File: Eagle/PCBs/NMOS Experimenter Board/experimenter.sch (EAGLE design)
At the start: 1182 parts, among them Q10 2N7002, Q11 2N7002, Q12 2N7002, Q13 2N7002, Q14 2N7002, Q15 2N7002, Q16 2N7002, Q17 2N7002, Q18 2N7002, Q19 2N7002, Q2 2N7002, Q20 2N7002, Q21 2N7002, Q22 2N7002, Q23 2N7002, Q24 2N7002, Q25 2N7002, Q26 2N7002, Q27 2N7002, Q28 2N7002, Q29 2N7002, Q3 2N7002, Q30 2N7002, Q31 2N7002, Q32 2N7002, Q33 2N7002, Q34 2N7002, Q35 2N7002, Q36 2N7002, Q37 2N7002, Q38 2N7002, Q39 2N7002, Q4 2N7002, Q40 2N7002, Q41 2N7002, Q42 2N7002, Q43 2N7002, Q44 2N7002, Q45 2N7002, Q46 2N7002, Q47 2N7002, Q48 2N7002, Q49 2N7002, Q5 2N7002, Q50 2N7002, Q51 2N7002, Q52 2N7002, Q53 2N7002, Q54 2N7002, Q55 2N7002, Q56 2N7002, Q57 2N7002, Q58 2N7002, Q59 2N7002, Q6 2N7002, Q60 2N7002, Q61 2N7002, Q62 2N7002, Q63 2N7002, Q64 2N7002, Q65 2N7002, Q66 2N7002, Q67 2N7002, Q68 2N7002, Q69 2N7002, Q7 2N7002, Q70 2N7002, Q71 2N7002, Q72 2N7002, Q73 2N7002, Q8 2N7002, Q9 2N7002, U1 74HC14PW

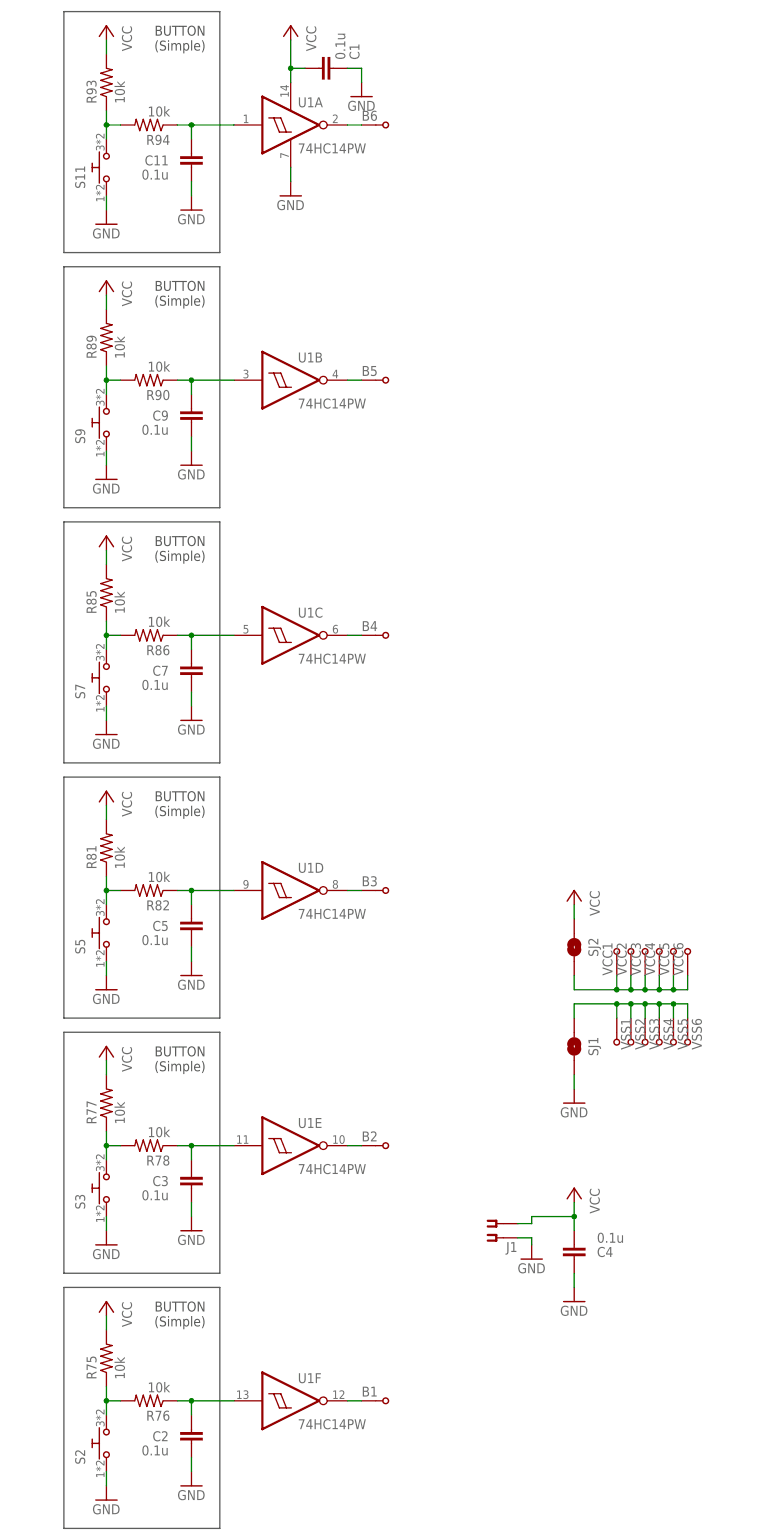
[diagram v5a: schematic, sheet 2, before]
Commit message: Added switches, preemptive first version
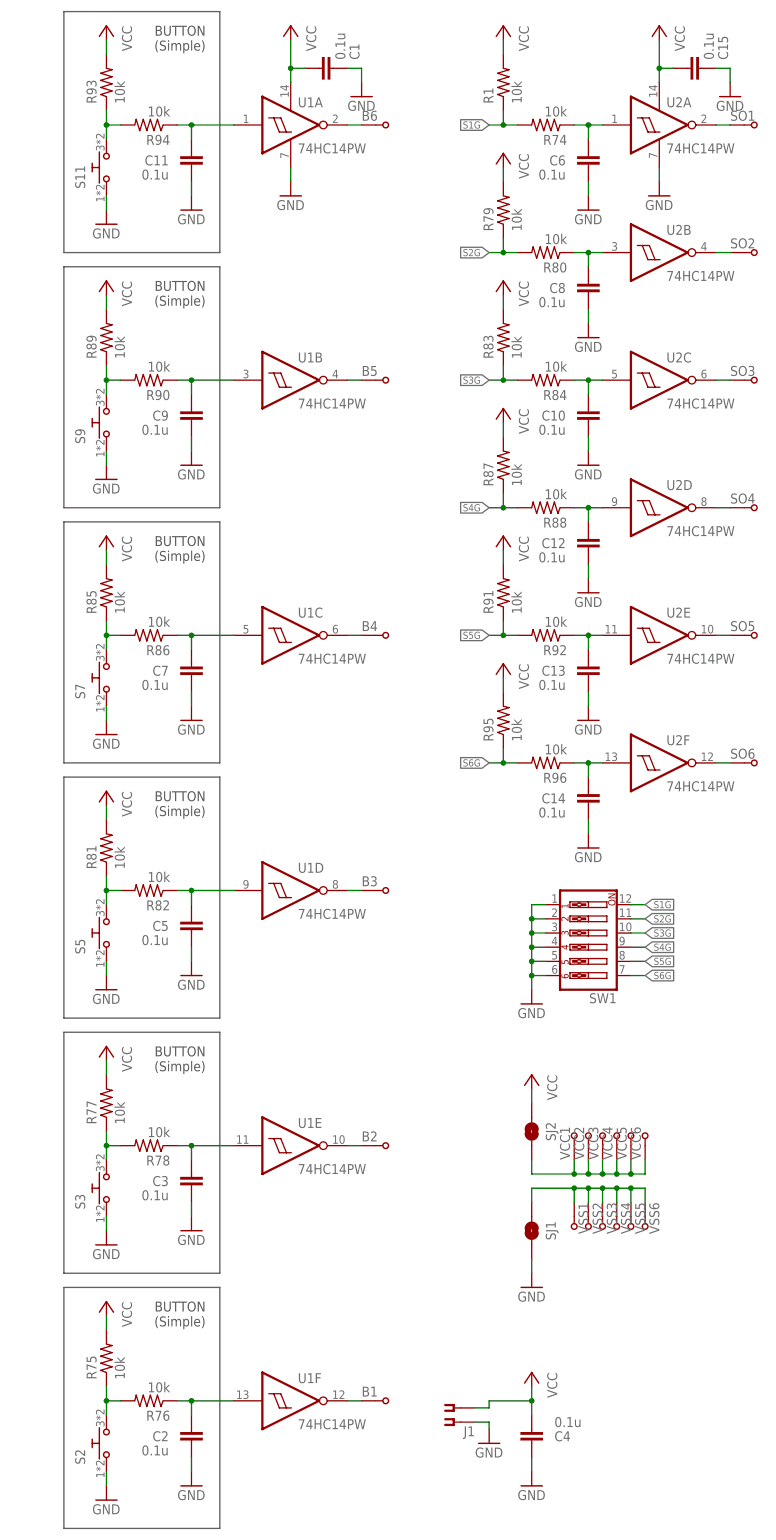
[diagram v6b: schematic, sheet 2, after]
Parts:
- added C10, C12, C13, C14, C15, C6, C8: 0.1u, ellajameson-core:CAP0603
- added R1, R74, R79, R80, R83, R84, R87, R88, R91, R92, R95, R96: 10k, ellajameson-core:RES0603
- added SO1, SO2, SO3, SO4, SO5, SO6: TPWIRE, ellajameson-core:TPWIRE
- added SW1: (no value), ellajameson-core:SW_DIP-6
- added U2: 74HC14PW, ellajameson-core:74HC14PW
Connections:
- new net N$307: SO6.S, U2F.O
- new net N$308: SO5.S, U2E.O
- new net N$311: SO4.S, U2D.O
- new net N$312: C8.1, R80.1, U2B.I
- new net N$313: SO3.S, U2C.O
- new net N$314: C10.1, R84.1, U2C.I
- new net N$315: SO2.S, U2B.O
- new net N$316: C12.1, R88.1, U2D.I
- new net N$317: SO1.S, U2A.O
- new net N$318: C13.1, R92.1, U2E.I
- new net N$320: C14.1, R96.1, U2F.I
- new net S1F: C6.1, R74.1, U2A.I
- new net S1G: R1.1, R74.2, SW1.12
- new net S2G: R79.1, R80.2, SW1.11
- new net S3G: R83.1, R84.2, SW1.10
- new net S4G: R87.1, R88.2, SW1.9
- new net S5G: R91.1, R92.2, SW1.8
- new net S6G: R95.1, R96.2, SW1.7
- net GND: now also C10.2, C12.2, C13.2, C14.2, C15.2, C6.2, C8.2, SW1.1, SW1.2, SW1.3, SW1.4, SW1.5, SW1.6, U2G$1.V-
- net VCC: now also C15.1, R1.2, R79.2, R83.2, R87.2, R91.2, R95.2, U2G$1.V+
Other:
- moved on the sheet: C4, J1, SJ1, SJ2, VCC1, VCC2, VCC3, VCC4, VCC5, VCC6, VSS1, VSS2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

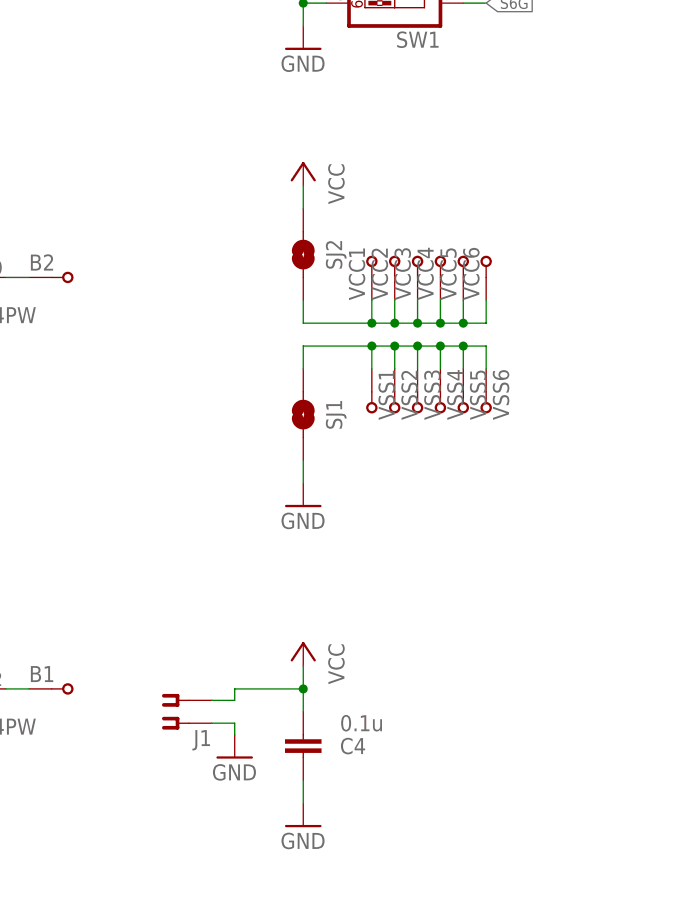
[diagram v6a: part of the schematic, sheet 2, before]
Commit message: Added amazing protoboard area.
https://www.eevblog.com/forum/manufacture/improved-protoboardperfboard-for-direct-soic-mounting/
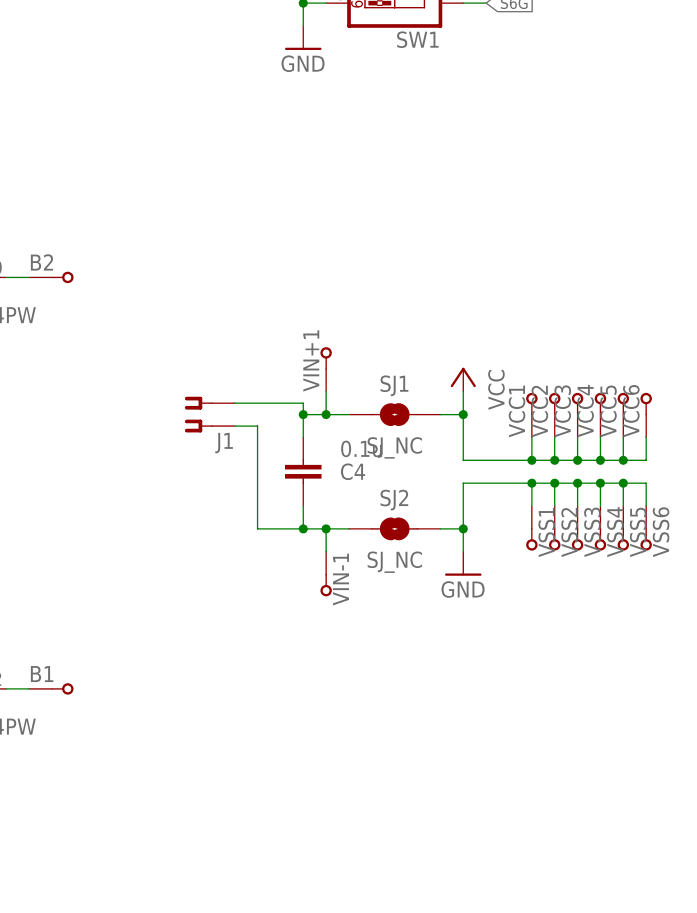
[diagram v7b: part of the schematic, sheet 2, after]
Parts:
- added VIN+1, VIN-1: TPWIRE, ellajameson-core:TPWIRE
- SJ1, SJ2: value SJ_NO -> SJ_NC; device ellajameson-core:SJ_NO -> ellajameson-core:SJ_NC
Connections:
- removed net N$303: SJ2.2, VCC1.S, VCC2.S, VCC3.S, VCC4.S, VCC5.S, VCC6.S
- removed net N$304: SJ1.1, VSS1.S, VSS2.S, VSS3.S, VSS4.S, VSS5.S, VSS6.S
- new net N$321: C4.1, J1.S, SJ2.1, VIN-1.S
- new net N$322: C4.2, J1.S1, SJ1.1, VIN+1.S
- net GND: now also SJ2.2, VSS1.S, VSS2.S, VSS3.S, VSS4.S, VSS5.S, VSS6.S; no longer C4.1, J1.S, SJ1.2
- net VCC: now also SJ1.2, VCC1.S, VCC2.S, VCC3.S, VCC4.S, VCC5.S, VCC6.S; no longer C4.2, J1.S1, SJ2.1
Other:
- moved on the sheet: C4, J1, SJ1, SJ2, VCC1, VCC2, VCC3, VCC4, VCC5, VCC6, VSS1, VSS2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

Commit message: Start rework on experimenter
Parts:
- removed C10, C12, C13, C14, C15, C6, C8: 0.1u, ellajameson-core:CAP0603
- removed D10, D11, D12, D13, D14, D15, D16, D17, D18, D19, D2, D20, D21, D22, D23, D24, D25, D26, D27, D28, D29, D3, D30, D31, D32, D33, D34, D35, D36, D37, D38, D39, D4, D40, D41, D42, D43, D44, D45, D46, D47, D48, D49, D5, D50, D51, D52, D53, D54, D55, D56, D57, D58, D59, D6, D60, D61, D62, D63, D64, D65, D66, D67, D68, D69, D7, D70, D71, D72, D73, D8, D9: (no value), ellajameson-core:LED0603
- removed DRAINA10, DRAINA11, DRAINA12, DRAINA13, DRAINA14, DRAINA15, DRAINA16, DRAINA17, DRAINA18, DRAINA19, DRAINA2, DRAINA20, DRAINA21, DRAINA22, DRAINA23, DRAINA24, DRAINA25, DRAINA26, DRAINA27, DRAINA28, DRAINA29, DRAINA3, DRAINA30, DRAINA31, DRAINA32, DRAINA33, DRAINA34, DRAINA35, DRAINA36, DRAINA37, DRAINA38, DRAINA39, DRAINA4, DRAINA40, DRAINA41, DRAINA42, DRAINA43, DRAINA44, DRAINA45, DRAINA46, DRAINA47, DRAINA48, DRAINA49, DRAINA5, DRAINA50, DRAINA51, DRAINA52, DRAINA53, DRAINA54, DRAINA55, DRAINA56, DRAINA57, DRAINA58, DRAINA59, DRAINA6, DRAINA60, DRAINA61, DRAINA62, DRAINA63, DRAINA64, DRAINA65, DRAINA66, DRAINA67, DRAINA68, DRAINA69, DRAINA7, DRAINA70, DRAINA71, DRAINA72, DRAINA73, DRAINA8, DRAINA9, DRAINB10, DRAINB11, DRAINB12, DRAINB13, DRAINB14, DRAINB15, DRAINB16, DRAINB17, DRAINB18, DRAINB19, DRAINB2, DRAINB20, DRAINB21, DRAINB22, DRAINB23, DRAINB24, DRAINB25, DRAINB26, DRAINB27, DRAINB28, DRAINB29, DRAINB3, DRAINB30, DRAINB31, DRAINB32, DRAINB33, DRAINB34, DRAINB35, DRAINB36, DRAINB37, DRAINB38, DRAINB39, DRAINB4, DRAINB40, DRAINB41, DRAINB42, DRAINB43, DRAINB44, DRAINB45, DRAINB46, DRAINB47, DRAINB48, DRAINB49, DRAINB5, DRAINB50, DRAINB51, DRAINB52, DRAINB53, DRAINB54, DRAINB55, DRAINB56, DRAINB57, DRAINB58, DRAINB59, DRAINB6, DRAINB60, DRAINB61, DRAINB62, DRAINB63, DRAINB64, DRAINB65, DRAINB66, DRAINB67, DRAINB68, DRAINB69, DRAINB7, DRAINB70, DRAINB71, DRAINB72, DRAINB73, DRAINB8, DRAINB9, DRAINC10, DRAINC11, DRAINC12, DRAINC13, DRAINC14, DRAINC15, DRAINC16, DRAINC17, DRAINC18, DRAINC19, DRAINC2, DRAINC20, DRAINC21, DRAINC22, DRAINC23, DRAINC24, DRAINC25, DRAINC26, DRAINC27, DRAINC28, DRAINC29, DRAINC3, DRAINC30, DRAINC31, DRAINC32, DRAINC33, DRAINC34, DRAINC35, DRAINC36, DRAINC37, DRAINC38, DRAINC39, DRAINC4, DRAINC40, DRAINC41, DRAINC42, DRAINC43, DRAINC44, DRAINC45, DRAINC46, DRAINC47, DRAINC48, DRAINC49, DRAINC5, DRAINC50, DRAINC51, DRAINC52, DRAINC53, DRAINC54, DRAINC55, DRAINC56, DRAINC57, DRAINC58, DRAINC59, DRAINC6, DRAINC60, DRAINC61, DRAINC62, DRAINC63, DRAINC64, DRAINC65, DRAINC66, DRAINC67, DRAINC68, DRAINC69, DRAINC7, DRAINC70, DRAINC71, DRAINC72, DRAINC73, DRAINC8, DRAINC9, DRAIND10, DRAIND11, DRAIND12, DRAIND13, DRAIND14, DRAIND15, DRAIND16, DRAIND17, DRAIND18, DRAIND19, DRAIND2, DRAIND20, DRAIND21, DRAIND22, DRAIND23, DRAIND24, DRAIND25, DRAIND26, DRAIND27, DRAIND28, DRAIND29, DRAIND3, DRAIND30, DRAIND31, DRAIND32, DRAIND33, DRAIND34, DRAIND35, DRAIND36, DRAIND37, DRAIND38, DRAIND39, DRAIND4, DRAIND40, DRAIND41, DRAIND42, DRAIND43, DRAIND44, DRAIND45, DRAIND46, DRAIND47, DRAIND48, DRAIND49, DRAIND5, DRAIND50, DRAIND51, DRAIND52, DRAIND53, DRAIND54, DRAIND55, DRAIND56, DRAIND57, DRAIND58, DRAIND59, DRAIND6, DRAIND60, DRAIND61, DRAIND62, DRAIND63, DRAIND64, DRAIND65, DRAIND66, DRAIND67, DRAIND68, DRAIND69, DRAIND7, DRAIND70, DRAIND71, DRAIND72, DRAIND73, DRAIND8, DRAIND9, GATE10, GATE11, GATE12, GATE13, GATE14, GATE15, GATE16, GATE17, GATE18, GATE19, GATE2, GATE20, GATE21, GATE22, GATE23, GATE24, GATE25, GATE26, GATE27, GATE28, GATE29, GATE3, GATE30, GATE31, GATE32, GATE33, GATE34, GATE35, GATE36, GATE37, GATE38, GATE39, GATE4, GATE40, GATE41, GATE42, GATE43, GATE44, GATE45, GATE46, GATE47, GATE48, GATE49, GATE5, GATE50, GATE51, GATE52, GATE53, GATE54, GATE55, GATE56, GATE57, GATE58, GATE59, GATE6, GATE60, GATE61, GATE62, GATE63, GATE64, GATE65, GATE66, GATE67, GATE68, GATE69, GATE7, GATE70, GATE71, GATE72, GATE73, GATE8, GATE9, SO1, SO2, SO3, SO4, SO5, SO6, SOURCEA10, SOURCEA11, SOURCEA12, SOURCEA13, SOURCEA14, SOURCEA15, SOURCEA16, SOURCEA17, SOURCEA18, SOURCEA19, SOURCEA2, SOURCEA20, SOURCEA21, SOURCEA22, SOURCEA23, SOURCEA24, SOURCEA25, SOURCEA26, SOURCEA27, SOURCEA28, SOURCEA29, SOURCEA3, SOURCEA30, SOURCEA31, SOURCEA32, SOURCEA33, SOURCEA34, SOURCEA35, SOURCEA36, SOURCEA37, SOURCEA38, SOURCEA39, SOURCEA4, SOURCEA40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: TPWIRE, ellajameson-core:TPWIRE
- removed JD10, JD11, JD12, JD13, JD14, JD17, JD18, JD19, JD2, JD20, JD21, JD22, JD23, JD24, JD25, JD26, JD27, JD28, JD29, JD3, JD30, JD31, JD32, JD33, JD34, JD35, JD36, JD37, JD38, JD39, JD4, JD40, JD41, JD42, JD43, JD44, JD45, JD46, JD47, JD48, JD49, JD5, JD50, JD51, JD52, JD53, JD54, JD55, JD56, JD57, JD58, JD59, JD6, JD60, JD61, JD62, JD63, JD64, JD65, JD66, JD68, JD7, JD70, JD72, JD8, JD9, JN10, JN11, JN12, JN13, JN14, JN15, JN16, JN17, JN18, JN19, JN2, JN20, JN21, JN22, JN23, JN24, JN25, JN26, JN27, JN28, JN29, JN3, JN30, JN31, JN32, JN33, JN34, JN35, JN36, JN37, JN38, JN39, JN4, JN40, JN41, JN42, JN43, JN44, JN45, JN46, JN47, JN48, JN49, JN5, JN50, JN51, JN52, JN53, JN54, JN55, JN56, JN57, JN58, JN59, JN6, JN60, JN61, JN62, JN63, JN64, JN65, JN66, JN67, JN68, JN69, JN7, JN70, JN71, JN72, JN73, JN8, JN9, JP10, JP11, JP12, JP13, JP14, JP15, JP16, JP17, JP18, JP19, JP2, JP20, JP21, JP22, JP23, JP24, JP25, JP26, JP27, JP28, JP29, JP3, JP30, JP31, JP32, JP33, JP34, JP35, JP36, JP37, JP38, JP39, JP4, JP40, JP41, JP42, JP43, JP44, JP45, JP46, JP47, JP48, JP49, JP5, JP50, JP51, JP52, JP53, JP54, JP55, JP56, JP57, JP58, JP59, JP6, JP60, JP61, JP62, JP63, JP64, JP65, JP66, JP67, JP68, JP69, JP7, JP70, JP71, JP72, JP73, JP8, JP9, JS10, JS11, JS12, JS13, JS16, JS17, JS26, JS27, JS28, JS29, JS30, JS31, JS32, JS33, JS34, JS35, JS36, JS37, JS38, JS39, JS4, JS40, JS41, JS42, JS43, JS44, JS45, JS46, JS47, JS48, JS49, JS5, JS50, JS51, JS52, JS53, JS54, JS55, JS56, JS57, JS58, JS59, JS6, JS60, JS61, JS62, JS63, JS64, JS65, JS66, JS67, JS68, JS69, JS7, JS70, JS71, JS72, JS73, JS8, JS9: SJ_NO, ellajameson-core:SJ_NO
- removed Q10, Q11, Q12, Q13, Q14, Q15, Q16, Q17, Q18, Q19, Q2, Q20, Q21, Q22, Q23, Q24, Q25, Q26, Q27, Q28, Q29, Q3, Q30, Q31, Q32, Q33, Q34, Q35, Q36, Q37, Q38, Q39, Q4, Q40, Q41, Q42, Q43, Q44, Q45, Q46, Q47, Q48, Q49, Q5, Q50, Q51, Q52, Q53, Q54, Q55, Q56, Q57, Q58, Q59, Q6, Q60, Q61, Q62, Q63, Q64, Q65, Q66, Q67, Q68, Q69, Q7, Q70, Q71, Q72, Q73, Q8, Q9: 2N7002, ellajameson-core:2N7002
- removed R1, R74, R79, R80, R83, R84, R87, R88, R91, R92, R95, R96: 10k, ellajameson-core:RES0603
- removed R10, R11, R12, R13, R14, R15, R16, R17, R18, R19, R2, R20, R21, R22, R23, R24, R25, R26, R27, R28, R29, R3, R30, R31, R32, R33, R34, R35, R36, R37, R38, R39, R4, R40, R41, R42, R43, R44, R45, R46, R47, R48, R49, R5, R50, R51, R52, R53, R54, R55, R56, R57, R58, R59, R6, R60, R61, R62, R63, R64, R65, R66, R67, R68, R69, R7, R70, R71, R72, R73, R8, R9: (no value), ellajameson-core:RES0603
- removed U2: 74HC14PW, ellajameson-core:74HC14PW
- B1, B2, B3, B4, B5, B6, VCC1, VCC2, VCC3, VIN+1, VIN-1, VSS1, VSS2, VSS3: value TPWIRE -> TPTHT; device ellajameson-core:TPWIRE -> ellajameson-core:TPTHT
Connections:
- removed net N$1: D2.A, JP2.2, R2.1
- removed net N$10: D3.K, DRAINA3.S, DRAINB3.S, DRAINC3.S, DRAIND3.S, JD2.1, JD3.2, JP3.1, JS5.1, Q3.D
- removed net N$100: GATE25.S, Q25.G
- removed net N$101: D26.A, JP26.2, R26.1
- removed net N$102: D26.K, DRAINA26.S, DRAINB26.S, DRAINC26.S, DRAIND26.S, JD26.2, JP26.1, JS34.1, Q26.D
- removed net N$103: JN26.2, JS26.2, Q26.S, SOURCEA26.S, SOURCEB26.S, SOURCEC26.S, SOURCED26.S
- removed net N$104: GATE26.S, Q26.G
- removed net N$105: D27.A, JP27.2, R27.1
- removed net N$106: D27.K, DRAINA27.S, DRAINB27.S, DRAINC27.S, DRAIND27.S, JD26.1, JD27.2, JP27.1, JS35.1, Q27.D
- removed net N$107: JN27.2, JS27.2, Q27.S, SOURCEA27.S, SOURCEB27.S, SOURCEC27.S, SOURCED27.S
- removed net N$108: GATE27.S, Q27.G
- removed net N$109: D28.A, JP28.2, R28.1
- removed net N$11: JN3.2, Q3.S, SOURCEA3.S, SOURCEB3.S, SOURCEC3.S, SOURCED3.S
- removed net N$110: D28.K, DRAINA28.S, DRAINB28.S, DRAINC28.S, DRAIND28.S, JD27.1, JD28.2, JP28.1, JS36.1, Q28.D
- removed net N$111: JN28.2, JS28.2, Q28.S, SOURCEA28.S, SOURCEB28.S, SOURCEC28.S, SOURCED28.S
- removed net N$112: GATE28.S, Q28.G
- removed net N$113: D29.A, JP29.2, R29.1
- removed net N$114: D29.K, DRAINA29.S, DRAINB29.S, DRAINC29.S, DRAIND29.S, JD28.1, JD29.2, JP29.1, JS37.1, Q29.D
- removed net N$115: JN29.2, JS29.2, Q29.S, SOURCEA29.S, SOURCEB29.S, SOURCEC29.S, SOURCED29.S
- removed net N$116: GATE29.S, Q29.G
- removed net N$117: D30.A, JP30.2, R30.1
- removed net N$118: D30.K, DRAINA30.S, DRAINB30.S, DRAINC30.S, DRAIND30.S, JD29.1, JD30.2, JP30.1, JS38.1, Q30.D
- removed net N$119: JN30.2, JS30.2, Q30.S, SOURCEA30.S, SOURCEB30.S, SOURCEC30.S, SOURCED30.S
- removed net N$12: GATE3.S, Q3.G
- removed net N$120: GATE30.S, Q30.G
- removed net N$121: D31.A, JP31.2, R31.1
- removed net N$122: D31.K, DRAINA31.S, DRAINB31.S, DRAINC31.S, DRAIND31.S, JD30.1, JD31.2, JP31.1, JS39.1, Q31.D
- removed net N$123: JN31.2, JS31.2, Q31.S, SOURCEA31.S, SOURCEB31.S, SOURCEC31.S, SOURCED31.S
- removed net N$124: GATE31.S, Q31.G
- removed net N$125: D32.A, JP32.2, R32.1
- removed net N$126: D32.K, DRAINA32.S, DRAINB32.S, DRAINC32.S, DRAIND32.S, JD31.1, JD32.2, JP32.1, JS40.1, Q32.D
- removed net N$127: JN32.2, JS32.2, Q32.S, SOURCEA32.S, SOURCEB32.S, SOURCEC32.S, SOURCED32.S
- removed net N$128: GATE32.S, Q32.G
- removed net N$129: D33.A, JP33.2, R33.1
- removed net N$13: D4.A, JP4.2, R4.1
- removed net N$130: D33.K, DRAINA33.S, DRAINB33.S, DRAINC33.S, DRAIND33.S, JD32.1, JD33.2, JP33.1, JS41.1, Q33.D
- removed net N$131: JN33.2, JS33.2, Q33.S, SOURCEA33.S, SOURCEB33.S, SOURCEC33.S, SOURCED33.S
- removed net N$132: GATE33.S, Q33.G
- removed net N$133: D34.A, JP34.2, R34.1
- removed net N$134: D34.K, DRAINA34.S, DRAINB34.S, DRAINC34.S, DRAIND34.S, JD34.2, JP34.1, JS42.1, Q34.D
- removed net N$135: JN34.2, JS34.2, Q34.S, SOURCEA34.S, SOURCEB34.S, SOURCEC34.S, SOURCED34.S
- removed net N$136: GATE34.S, Q34.G
- removed net N$137: D35.A, JP35.2, R35.1
- removed net N$138: D35.K, DRAINA35.S, DRAINB35.S, DRAINC35.S, DRAIND35.S, JD34.1, JD35.2, JP35.1, JS43.1, Q35.D
- removed net N$139: JN35.2, JS35.2, Q35.S, SOURCEA35.S, SOURCEB35.S, SOURCEC35.S, SOURCED35.S
- removed net N$14: D4.K, DRAINA4.S, DRAINB4.S, DRAINC4.S, DRAIND4.S, JD33.1, JD4.2, JP4.1, JS6.1, Q4.D
- removed net N$140: GATE35.S, Q35.G
- removed net N$141: D36.A, JP36.2, R36.1
- removed net N$142: D36.K, DRAINA36.S, DRAINB36.S, DRAINC36.S, DRAIND36.S, JD35.1, JD36.2, JP36.1, JS44.1, Q36.D
- removed net N$143: JN36.2, JS36.2, Q36.S, SOURCEA36.S, SOURCEB36.S, SOURCEC36.S, SOURCED36.S
- removed net N$144: GATE36.S, Q36.G
- removed net N$145: D37.A, JP37.2, R37.1
- removed net N$146: D37.K, DRAINA37.S, DRAINB37.S, DRAINC37.S, DRAIND37.S, JD36.1, JD37.2, JP37.1, JS45.1, Q37.D
- removed net N$147: JN37.2, JS37.2, Q37.S, SOURCEA37.S, SOURCEB37.S, SOURCEC37.S, SOURCED37.S
- removed net N$148: GATE37.S, Q37.G
- removed net N$149: D38.A, JP38.2, R38.1
- removed net N$15: JN4.2, JS4.2, Q4.S, SOURCEA4.S, SOURCEB4.S, SOURCEC4.S, SOURCED4.S
- removed net N$150: D38.K, DRAINA38.S, DRAINB38.S, DRAINC38.S, DRAIND38.S, JD37.1, JD38.2, JP38.1, JS46.1, Q38.D
- removed net N$151: JN38.2, JS38.2, Q38.S, SOURCEA38.S, SOURCEB38.S, SOURCEC38.S, SOURCED38.S
- removed net N$152: GATE38.S, Q38.G
- removed net N$153: D39.A, JP39.2, R39.1
- removed net N$154: D39.K, DRAINA39.S, DRAINB39.S, DRAINC39.S, DRAIND39.S, JD38.1, JD39.2, JP39.1, JS47.1, Q39.D
- removed net N$155: JN39.2, JS39.2, Q39.S, SOURCEA39.S, SOURCEB39.S, SOURCEC39.S, SOURCED39.S
- removed net N$156: GATE39.S, Q39.G
- removed net N$157: D40.A, JP40.2, R40.1
- removed net N$158: D40.K, DRAINA40.S, DRAINB40.S, DRAINC40.S, DRAIND40.S, JD39.1, JD40.2, JP40.1, JS48.1, Q40.D
- removed net N$159: JN40.2, JS40.2, Q40.S, SOURCEA40.S, SOURCEB40.S, SOURCEC40.S, SOURCED40.S
- removed net N$16: GATE4.S, Q4.G
- removed net N$160: GATE40.S, Q40.G
- removed net N$161: D41.A, JP41.2, R41.1
- removed net N$162: D41.K, DRAINA41.S, DRAINB41.S, DRAINC41.S, DRAIND41.S, JD40.1, JD41.2, JP41.1, JS49.1, Q41.D
- removed net N$163: JN41.2, JS41.2, Q41.S, SOURCEA41.S, SOURCEB41.S, SOURCEC41.S, SOURCED41.S
- removed net N$164: GATE41.S, Q41.G
- removed net N$165: D42.A, JP42.2, R42.1
- removed net N$166: D42.K, DRAINA42.S, DRAINB42.S, DRAINC42.S, DRAIND42.S, JD42.2, JP42.1, JS50.1, Q42.D
- removed net N$167: JN42.2, JS42.2, Q42.S, SOURCEA42.S, SOURCEB42.S, SOURCEC42.S, SOURCED42.S
- removed net N$168: GATE42.S, Q42.G
- removed net N$169: D43.A, JP43.2, R43.1
- removed net N$17: D5.A, JP5.2, R5.1
- removed net N$170: D43.K, DRAINA43.S, DRAINB43.S, DRAINC43.S, DRAIND43.S, JD42.1, JD43.2, JP43.1, JS51.1, Q43.D
- removed net N$171: JN43.2, JS43.2, Q43.S, SOURCEA43.S, SOURCEB43.S, SOURCEC43.S, SOURCED43.S
- removed net N$172: GATE43.S, Q43.G
- removed net N$173: D44.A, JP44.2, R44.1
- removed net N$174: D44.K, DRAINA44.S, DRAINB44.S, DRAINC44.S, DRAIND44.S, JD43.1, JD44.2, JP44.1, JS52.1, Q44.D
- removed net N$175: JN44.2, JS44.2, Q44.S, SOURCEA44.S, SOURCEB44.S, SOURCEC44.S, SOURCED44.S
- removed net N$176: GATE44.S, Q44.G
- removed net N$177: D45.A, JP45.2, R45.1
- removed net N$178: D45.K, DRAINA45.S, DRAINB45.S, DRAINC45.S, DRAIND45.S, JD44.1, JD45.2, JP45.1, JS53.1, Q45.D
- removed net N$179: JN45.2, JS45.2, Q45.S, SOURCEA45.S, SOURCEB45.S, SOURCEC45.S, SOURCED45.S
- removed net N$18: D5.K, DRAINA5.S, DRAINB5.S, DRAINC5.S, DRAIND5.S, JD4.1, JD5.2, JP5.1, JS7.1, Q5.D
- removed net N$180: GATE45.S, Q45.G
- removed net N$181: D46.A, JP46.2, R46.1
- removed net N$182: D46.K, DRAINA46.S, DRAINB46.S, DRAINC46.S, DRAIND46.S, JD45.1, JD46.2, JP46.1, JS54.1, Q46.D
- removed net N$183: JN46.2, JS46.2, Q46.S, SOURCEA46.S, SOURCEB46.S, SOURCEC46.S, SOURCED46.S
- removed net N$184: GATE46.S, Q46.G
- removed net N$185: D47.A, JP47.2, R47.1
- removed net N$186: D47.K, DRAINA47.S, DRAINB47.S, DRAINC47.S, DRAIND47.S, JD46.1, JD47.2, JP47.1, JS55.1, Q47.D
- removed net N$187: JN47.2, JS47.2, Q47.S, SOURCEA47.S, SOURCEB47.S, SOURCEC47.S, SOURCED47.S
- removed net N$188: GATE47.S, Q47.G
- removed net N$189: D48.A, JP48.2, R48.1
- removed net N$19: JN5.2, JS5.2, Q5.S, SOURCEA5.S, SOURCEB5.S, SOURCEC5.S, SOURCED5.S
- removed net N$190: D48.K, DRAINA48.S, DRAINB48.S, DRAINC48.S, DRAIND48.S, JD47.1, JD48.2, JP48.1, JS56.1, Q48.D
- removed net N$191: JN48.2, JS48.2, Q48.S, SOURCEA48.S, SOURCEB48.S, SOURCEC48.S, SOURCED48.S
- removed net N$192: GATE48.S, Q48.G
- removed net N$193: D49.A, JP49.2, R49.1
- removed net N$194: D49.K, DRAINA49.S, DRAINB49.S, DRAINC49.S, DRAIND49.S, JD48.1, JD49.2, JP49.1, JS57.1, Q49.D
- removed net N$195: JN49.2, JS49.2, Q49.S, SOURCEA49.S, SOURCEB49.S, SOURCEC49.S, SOURCED49.S
- removed net N$196: GATE49.S, Q49.G
- removed net N$197: D50.A, JP50.2, R50.1
- removed net N$198: D50.K, DRAINA50.S, DRAINB50.S, DRAINC50.S, DRAIND50.S, JD50.2, JP50.1, JS58.1, Q50.D
- removed net N$199: JN50.2, JS50.2, Q50.S, SOURCEA50.S, SOURCEB50.S, SOURCEC50.S, SOURCED50.S
- removed net N$2: D2.K, DRAINA2.S, DRAINB2.S, DRAINC2.S, DRAIND2.S, JD2.2, JD25.1, JP2.1, JS4.1, Q2.D
- removed net N$20: GATE5.S, Q5.G
- removed net N$200: GATE50.S, Q50.G
- removed net N$201: D51.A, JP51.2, R51.1
- removed net N$202: D51.K, DRAINA51.S, DRAINB51.S, DRAINC51.S, DRAIND51.S, JD50.1, JD51.2, JP51.1, JS59.1, Q51.D
- removed net N$203: JN51.2, JS51.2, Q51.S, SOURCEA51.S, SOURCEB51.S, SOURCEC51.S, SOURCED51.S
- removed net N$204: GATE51.S, Q51.G
- removed net N$205: D52.A, JP52.2, R52.1
- removed net N$206: D52.K, DRAINA52.S, DRAINB52.S, DRAINC52.S, DRAIND52.S, JD51.1, JD52.2, JP52.1, JS60.1, Q52.D
- removed net N$207: JN52.2, JS52.2, Q52.S, SOURCEA52.S, SOURCEB52.S, SOURCEC52.S, SOURCED52.S
- removed net N$208: GATE52.S, Q52.G
- removed net N$209: D53.A, JP53.2, R53.1
- removed net N$21: D6.A, JP6.2, R6.1
- removed net N$210: D53.K, DRAINA53.S, DRAINB53.S, DRAINC53.S, DRAIND53.S, JD52.1, JD53.2, JP53.1, JS61.1, Q53.D
- removed net N$211: JN53.2, JS53.2, Q53.S, SOURCEA53.S, SOURCEB53.S, SOURCEC53.S, SOURCED53.S
- removed net N$212: GATE53.S, Q53.G
- removed net N$213: D54.A, JP54.2, R54.1
- removed net N$214: D54.K, DRAINA54.S, DRAINB54.S, DRAINC54.S, DRAIND54.S, JD53.1, JD54.2, JP54.1, JS62.1, Q54.D
- removed net N$215: JN54.2, JS54.2, Q54.S, SOURCEA54.S, SOURCEB54.S, SOURCEC54.S, SOURCED54.S
- removed net N$216: GATE54.S, Q54.G
- removed net N$217: D55.A, JP55.2, R55.1
- removed net N$218: D55.K, DRAINA55.S, DRAINB55.S, DRAINC55.S, DRAIND55.S, JD54.1, JD55.2, JP55.1, JS63.1, Q55.D
- removed net N$219: JN55.2, JS55.2, Q55.S, SOURCEA55.S, SOURCEB55.S, SOURCEC55.S, SOURCED55.S
- removed net N$22: D6.K, DRAINA6.S, DRAINB6.S, DRAINC6.S, DRAIND6.S, JD41.1, JD6.2, JP6.1, JS8.1, Q6.D
- removed net N$220: GATE55.S, Q55.G
- removed net N$221: D56.A, JP56.2, R56.1
- removed net N$222: D56.K, DRAINA56.S, DRAINB56.S, DRAINC56.S, DRAIND56.S, JD55.1, JD56.2, JP56.1, JS64.1, Q56.D
- removed net N$223: JN56.2, JS56.2, Q56.S, SOURCEA56.S, SOURCEB56.S, SOURCEC56.S, SOURCED56.S
- removed net N$224: GATE56.S, Q56.G
- removed net N$225: D57.A, JP57.2, R57.1
- removed net N$226: D57.K, DRAINA57.S, DRAINB57.S, DRAINC57.S, DRAIND57.S, JD56.1, JD57.2, JP57.1, JS65.1, Q57.D
- removed net N$227: JN57.2, JS57.2, Q57.S, SOURCEA57.S, SOURCEB57.S, SOURCEC57.S, SOURCED57.S
- removed net N$228: GATE57.S, Q57.G
- removed net N$229: D58.A, JP58.2, R58.1
- removed net N$23: JN6.2, JS6.2, Q6.S, SOURCEA6.S, SOURCEB6.S, SOURCEC6.S, SOURCED6.S
- removed net N$230: D58.K, DRAINA58.S, DRAINB58.S, DRAINC58.S, DRAIND58.S, JD58.2, JP58.1, Q58.D
- removed net N$231: JN58.2, JS58.2, Q58.S, SOURCEA58.S, SOURCEB58.S, SOURCEC58.S, SOURCED58.S
- removed net N$232: GATE58.S, Q58.G
- removed net N$233: D59.A, JP59.2, R59.1
- removed net N$234: D59.K, DRAINA59.S, DRAINB59.S, DRAINC59.S, DRAIND59.S, JD58.1, JD59.2, JP59.1, Q59.D
- removed net N$235: JN59.2, JS59.2, Q59.S, SOURCEA59.S, SOURCEB59.S, SOURCEC59.S, SOURCED59.S
- removed net N$236: GATE59.S, Q59.G
- removed net N$237: D60.A, JP60.2, R60.1
- removed net N$238: D60.K, DRAINA60.S, DRAINB60.S, DRAINC60.S, DRAIND60.S, JD59.1, JD60.2, JP60.1, Q60.D
- removed net N$239: JN60.2, JS60.2, Q60.S, SOURCEA60.S, SOURCEB60.S, SOURCEC60.S, SOURCED60.S
- removed net N$24: GATE6.S, Q6.G
- removed net N$240: GATE60.S, Q60.G
- removed net N$241: D61.A, JP61.2, R61.1
- removed net N$242: D61.K, DRAINA61.S, DRAINB61.S, DRAINC61.S, DRAIND61.S, JD60.1, JD61.2, JP61.1, Q61.D
- removed net N$243: JN61.2, JS61.2, Q61.S, SOURCEA61.S, SOURCEB61.S, SOURCEC61.S, SOURCED61.S
- removed net N$244: GATE61.S, Q61.G
- removed net N$245: D62.A, JP62.2, R62.1
- removed net N$246: D62.K, DRAINA62.S, DRAINB62.S, DRAINC62.S, DRAIND62.S, JD61.1, JD62.2, JP62.1, Q62.D
- removed net N$247: JN62.2, JS62.2, Q62.S, SOURCEA62.S, SOURCEB62.S, SOURCEC62.S, SOURCED62.S
- removed net N$248: GATE62.S, Q62.G
- removed net N$249: D63.A, JP63.2, R63.1
- removed net N$25: D7.A, JP7.2, R7.1
- removed net N$250: D63.K, DRAINA63.S, DRAINB63.S, DRAINC63.S, DRAIND63.S, JD62.1, JD63.2, JP63.1, Q63.D
- removed net N$251: JN63.2, JS63.2, Q63.S, SOURCEA63.S, SOURCEB63.S, SOURCEC63.S, SOURCED63.S
- removed net N$252: GATE63.S, Q63.G
- removed net N$253: D64.A, JP64.2, R64.1
- removed net N$254: D64.K, DRAINA64.S, DRAINB64.S, DRAINC64.S, DRAIND64.S, JD63.1, JD64.2, JP64.1, Q64.D
- removed net N$255: JN64.2, JS64.2, Q64.S, SOURCEA64.S, SOURCEB64.S, SOURCEC64.S, SOURCED64.S
- removed net N$256: GATE64.S, Q64.G
- removed net N$257: D65.A, JP65.2, R65.1
- removed net N$258: D65.K, DRAINA65.S, DRAINB65.S, DRAINC65.S, DRAIND65.S, JD64.1, JD65.2, JP65.1, Q65.D
- removed net N$259: JN65.2, JS65.2, Q65.S, SOURCEA65.S, SOURCEB65.S, SOURCEC65.S, SOURCED65.S
- removed net N$26: D7.K, DRAINA7.S, DRAINB7.S, DRAINC7.S, DRAIND7.S, JD6.1, JD7.2, JP7.1, JS9.1, Q7.D
- removed net N$260: GATE65.S, Q65.G
- removed net N$261: D66.A, JP66.2, R66.1
- removed net N$262: D66.K, DRAINA66.S, DRAINB66.S, DRAINC66.S, DRAIND66.S, JD66.2, JD7.1, JP66.1, JS68.1, Q66.D
- removed net N$263: JN66.2, JS66.2, Q66.S, SOURCEA66.S, SOURCEB66.S, SOURCEC66.S, SOURCED66.S
- removed net N$264: GATE66.S, Q66.G
- removed net N$265: D67.A, JP67.2, R67.1
- removed net N$266: D67.K, DRAINA67.S, DRAINB67.S, DRAINC67.S, DRAIND67.S, JD66.1, JP67.1, JS69.1, Q67.D
- removed net N$267: JN67.2, JS67.2, Q67.S, SOURCEA67.S, SOURCEB67.S, SOURCEC67.S, SOURCED67.S
- removed net N$268: GATE67.S, Q67.G
- removed net N$269: D68.A, JP68.2, R68.1
- removed net N$27: JN7.2, JS7.2, Q7.S, SOURCEA7.S, SOURCEB7.S, SOURCEC7.S, SOURCED7.S
- removed net N$270: D68.K, DRAINA68.S, DRAINB68.S, DRAINC68.S, DRAIND68.S, JD68.2, JD9.1, JP68.1, JS70.1, Q68.D
- removed net N$271: JN68.2, JS68.2, Q68.S, SOURCEA68.S, SOURCEB68.S, SOURCEC68.S, SOURCED68.S
- removed net N$272: GATE68.S, Q68.G
- removed net N$273: D69.A, JP69.2, R69.1
- removed net N$274: D69.K, DRAINA69.S, DRAINB69.S, DRAINC69.S, DRAIND69.S, JD68.1, JP69.1, JS71.1, Q69.D
- removed net N$275: JN69.2, JS69.2, Q69.S, SOURCEA69.S, SOURCEB69.S, SOURCEC69.S, SOURCED69.S
- removed net N$276: GATE69.S, Q69.G
- removed net N$277: D70.A, JP70.2, R70.1
- removed net N$278: D70.K, DRAINA70.S, DRAINB70.S, DRAINC70.S, DRAIND70.S, JD11.1, JD70.2, JP70.1, JS72.1, Q70.D
- removed net N$279: JN70.2, JS70.2, Q70.S, SOURCEA70.S, SOURCEB70.S, SOURCEC70.S, SOURCED70.S
- removed net N$28: GATE7.S, Q7.G
- removed net N$280: GATE70.S, Q70.G
- removed net N$281: D71.A, JP71.2, R71.1
- removed net N$282: D71.K, DRAINA71.S, DRAINB71.S, DRAINC71.S, DRAIND71.S, JD70.1, JP71.1, JS73.1, Q71.D
- removed net N$283: JN71.2, JS71.2, Q71.S, SOURCEA71.S, SOURCEB71.S, SOURCEC71.S, SOURCED71.S
- removed net N$284: GATE71.S, Q71.G
- removed net N$285: D72.A, JP72.2, R72.1
- removed net N$286: D72.K, DRAINA72.S, DRAINB72.S, DRAINC72.S, DRAIND72.S, JD13.1, JD72.2, JP72.1, Q72.D
- removed net N$287: JN72.2, JS72.2, Q72.S, SOURCEA72.S, SOURCEB72.S, SOURCEC72.S, SOURCED72.S
- removed net N$288: GATE72.S, Q72.G
- removed net N$289: D73.A, JP73.2, R73.1
- removed net N$29: D8.A, JP8.2, R8.1
- removed net N$290: D73.K, DRAINA73.S, DRAINB73.S, DRAINC73.S, DRAIND73.S, JD72.1, JP73.1, Q73.D
- removed net N$291: JN73.2, JS73.2, Q73.S, SOURCEA73.S, SOURCEB73.S, SOURCEC73.S, SOURCED73.S
- removed net N$292: GATE73.S, Q73.G
- removed net N$293: R77.1, R78.2, S3.S
- removed net N$297: R81.1, R82.2, S5.S
- removed net N$3: JN2.2, Q2.S, SOURCEA2.S, SOURCEB2.S, SOURCEC2.S, SOURCED2.S
- removed net N$30: D8.K, DRAINA8.S, DRAINB8.S, DRAINC8.S, DRAIND8.S, JD49.1, JD8.2, JP8.1, JS10.1, Q8.D
- removed net N$301: R85.1, R86.2, S7.S
- removed net N$305: R89.1, R90.2, S9.S
- removed net N$307: SO6.S, U2F.O
- removed net N$308: SO5.S, U2E.O
- removed net N$309: R93.1, R94.2, S11.S
- removed net N$31: JN8.2, JS8.2, Q8.S, SOURCEA8.S, SOURCEB8.S, SOURCEC8.S, SOURCED8.S
- removed net N$311: SO4.S, U2D.O
- removed net N$312: C8.1, R80.1, U2B.I
- removed net N$313: SO3.S, U2C.O
- removed net N$314: C10.1, R84.1, U2C.I
- removed net N$315: SO2.S, U2B.O
- removed net N$316: C12.1, R88.1, U2D.I
- removed net N$317: SO1.S, U2A.O
- removed net N$318: C13.1, R92.1, U2E.I
- removed net N$32: GATE8.S, Q8.G
- removed net N$320: C14.1, R96.1, U2F.I
- removed net N$33: D9.A, JP9.2, R9.1
- removed net N$34: D9.K, DRAINA9.S, DRAINB9.S, DRAINC9.S, DRAIND9.S, JD8.1, JD9.2, JP9.1, JS11.1, Q9.D
- removed net N$35: JN9.2, JS9.2, Q9.S, SOURCEA9.S, SOURCEB9.S, SOURCEC9.S, SOURCED9.S
- removed net N$36: GATE9.S, Q9.G
- removed net N$37: D10.A, JP10.2, R10.1
- removed net N$38: D10.K, DRAINA10.S, DRAINB10.S, DRAINC10.S, DRAIND10.S, JD10.2, JD57.1, JP10.1, JS12.1, Q10.D
- removed net N$39: JN10.2, JS10.2, Q10.S, SOURCEA10.S, SOURCEB10.S, SOURCEC10.S, SOURCED10.S
- removed net N$4: GATE2.S, Q2.G
- removed net N$40: GATE10.S, Q10.G
- removed net N$41: D11.A, JP11.2, R11.1
- removed net N$42: D11.K, DRAINA11.S, DRAINB11.S, DRAINC11.S, DRAIND11.S, JD10.1, JD11.2, JP11.1, JS13.1, Q11.D
- removed net N$43: JN11.2, JS11.2, Q11.S, SOURCEA11.S, SOURCEB11.S, SOURCEC11.S, SOURCED11.S
- removed net N$44: GATE11.S, Q11.G
- removed net N$45: D12.A, JP12.2, R12.1
- removed net N$46: D12.K, DRAINA12.S, DRAINB12.S, DRAINC12.S, DRAIND12.S, JD12.2, JD65.1, JP12.1, Q12.D
- removed net N$47: JN12.2, JS12.2, Q12.S, SOURCEA12.S, SOURCEB12.S, SOURCEC12.S, SOURCED12.S
- removed net N$48: GATE12.S, Q12.G
- removed net N$49: D13.A, JP13.2, R13.1
- removed net N$50: D13.K, DRAINA13.S, DRAINB13.S, DRAINC13.S, DRAIND13.S, JD12.1, JD13.2, JP13.1, Q13.D
- removed net N$51: JN13.2, JS13.2, Q13.S, SOURCEA13.S, SOURCEB13.S, SOURCEC13.S, SOURCED13.S
- removed net N$52: GATE13.S, Q13.G
- removed net N$53: D14.A, JP14.2, R14.1
- removed net N$54: D14.K, DRAINA14.S, DRAINB14.S, DRAINC14.S, DRAIND14.S, JD14.2, JD3.1, JP14.1, JS17.1, Q14.D
- removed net N$55: JN14.2, Q14.S, SOURCEA14.S, SOURCEB14.S, SOURCEC14.S, SOURCED14.S
- removed net N$56: GATE14.S, Q14.G
- removed net N$57: D15.A, JP15.2, R15.1
- removed net N$58: D15.K, DRAINA15.S, DRAINB15.S, DRAINC15.S, DRAIND15.S, JD14.1, JP15.1, JS16.1, Q15.D
- removed net N$59: JN15.2, Q15.S, SOURCEA15.S, SOURCEB15.S, SOURCEC15.S, SOURCED15.S
- removed net N$60: GATE15.S, Q15.G
- removed net N$61: D16.A, JP16.2, R16.1
- removed net N$62: D16.K, DRAINA16.S, DRAINB16.S, DRAINC16.S, DRAIND16.S, JD17.1, JP16.1, JS67.1, Q16.D
- removed net N$63: JN16.2, JS16.2, Q16.S, SOURCEA16.S, SOURCEB16.S, SOURCEC16.S, SOURCED16.S
- removed net N$64: GATE16.S, Q16.G
- removed net N$65: D17.A, JP17.2, R17.1
- removed net N$66: D17.K, DRAINA17.S, DRAINB17.S, DRAINC17.S, DRAIND17.S, JD17.2, JD5.1, JP17.1, JS66.1, Q17.D
- removed net N$67: JN17.2, JS17.2, Q17.S, SOURCEA17.S, SOURCEB17.S, SOURCEC17.S, SOURCED17.S
- removed net N$68: GATE17.S, Q17.G
- removed net N$69: D18.A, JP18.2, R18.1
- removed net N$7: R75.1, R76.2, S2.S
- removed net N$70: D18.K, DRAINA18.S, DRAINB18.S, DRAINC18.S, DRAIND18.S, JD18.2, JP18.1, JS26.1, Q18.D
- removed net N$71: JN18.2, Q18.S, SOURCEA18.S, SOURCEB18.S, SOURCEC18.S, SOURCED18.S
- removed net N$72: GATE18.S, Q18.G
- removed net N$73: D19.A, JP19.2, R19.1
- removed net N$74: D19.K, DRAINA19.S, DRAINB19.S, DRAINC19.S, DRAIND19.S, JD18.1, JD19.2, JP19.1, JS27.1, Q19.D
- removed net N$75: JN19.2, Q19.S, SOURCEA19.S, SOURCEB19.S, SOURCEC19.S, SOURCED19.S
- removed net N$76: GATE19.S, Q19.G
- removed net N$77: D20.A, JP20.2, R20.1
- removed net N$78: D20.K, DRAINA20.S, DRAINB20.S, DRAINC20.S, DRAIND20.S, JD19.1, JD20.2, JP20.1, JS28.1, Q20.D
- removed net N$79: JN20.2, Q20.S, SOURCEA20.S, SOURCEB20.S, SOURCEC20.S, SOURCED20.S
- removed net N$80: GATE20.S, Q20.G
- removed net N$81: D21.A, JP21.2, R21.1
- removed net N$82: D21.K, DRAINA21.S, DRAINB21.S, DRAINC21.S, DRAIND21.S, JD20.1, JD21.2, JP21.1, JS29.1, Q21.D
- removed net N$83: JN21.2, Q21.S, SOURCEA21.S, SOURCEB21.S, SOURCEC21.S, SOURCED21.S
- removed net N$84: GATE21.S, Q21.G
- removed net N$85: D22.A, JP22.2, R22.1
- removed net N$86: D22.K, DRAINA22.S, DRAINB22.S, DRAINC22.S, DRAIND22.S, JD21.1, JD22.2, JP22.1, JS30.1, Q22.D
- removed net N$87: JN22.2, Q22.S, SOURCEA22.S, SOURCEB22.S, SOURCEC22.S, SOURCED22.S
- removed net N$88: GATE22.S, Q22.G
- removed net N$89: D23.A, JP23.2, R23.1
- removed net N$9: D3.A, JP3.2, R3.1
- removed net N$90: D23.K, DRAINA23.S, DRAINB23.S, DRAINC23.S, DRAIND23.S, JD22.1, JD23.2, JP23.1, JS31.1, Q23.D
- removed net N$91: JN23.2, Q23.S, SOURCEA23.S, SOURCEB23.S, SOURCEC23.S, SOURCED23.S
- removed net N$92: GATE23.S, Q23.G
- removed net N$93: D24.A, JP24.2, R24.1
- removed net N$94: D24.K, DRAINA24.S, DRAINB24.S, DRAINC24.S, DRAIND24.S, JD23.1, JD24.2, JP24.1, JS32.1, Q24.D
- removed net N$95: JN24.2, Q24.S, SOURCEA24.S, SOURCEB24.S, SOURCEC24.S, SOURCED24.S
- removed net N$96: GATE24.S, Q24.G
- removed net N$97: D25.A, JP25.2, R25.1
- removed net N$98: D25.K, DRAINA25.S, DRAINB25.S, DRAINC25.S, DRAIND25.S, JD24.1, JD25.2, JP25.1, JS33.1, Q25.D
- removed net N$99: JN25.2, Q25.S, SOURCEA25.S, SOURCEB25.S, SOURCEC25.S, SOURCED25.S
- removed net S1F: C6.1, R74.1, U2A.I
- net GND: no longer C10.2, C12.2, C13.2, C14.2, C15.2, C6.2, C8.2, JN10.1, JN11.1, JN12.1, JN13.1, JN14.1, JN15.1, JN16.1, JN17.1, JN18.1, JN19.1, JN2.1, JN20.1, JN21.1, JN22.1, JN23.1, JN24.1, JN25.1, JN26.1, JN27.1, JN28.1, JN29.1, JN3.1, JN30.1, JN31.1, JN32.1, JN33.1, JN34.1, JN35.1, JN36.1, JN37.1, JN38.1, JN39.1, JN4.1, JN40.1, JN41.1, JN42.1, JN43.1, JN44.1, JN45.1, JN46.1, JN47.1, JN48.1, JN49.1, JN5.1, JN50.1, JN51.1, JN52.1, JN53.1, JN54.1, JN55.1, JN56.1, JN57.1, JN58.1, JN59.1, JN6.1, JN60.1, JN61.1, JN62.1, JN63.1, JN64.1, JN65.1, JN66.1, JN67.1, JN68.1, JN69.1, JN7.1, JN70.1, JN71.1, JN72.1, JN73.1, JN8.1, JN9.1, U2G$1.V-, VSS4.S, VSS5.S, VSS6.S
- net S1G: now also R75.1, R76.2, S2.S; no longer R1.1, R74.2
- net S2G: now also R77.1, R78.2, S3.S; no longer R79.1, R80.2
- net S3G: now also R81.1, R82.2, S5.S; no longer R83.1, R84.2
- net S4G: now also R85.1, R86.2, S7.S; no longer R87.1, R88.2
- net S5G: now also R89.1, R90.2, S9.S; no longer R91.1, R92.2
- net S6G: now also R93.1, R94.2, S11.S; no longer R95.1, R96.2
- net VCC: no longer C15.1, R1.2, R10.2, R11.2, R12.2, R13.2, R14.2, R15.2, R16.2, R17.2, R18.2, R19.2, R2.2, R20.2, R21.2, R22.2, R23.2, R24.2, R25.2, R26.2, R27.2, R28.2, R29.2, R3.2, R30.2, R31.2, R32.2, R33.2, R34.2, R35.2, R36.2, R37.2, R38.2, R39.2, R4.2, R40.2, R41.2, R42.2, R43.2, R44.2, R45.2, R46.2, R47.2, R48.2, R49.2, R5.2, R50.2, R51.2, R52.2, R53.2, R54.2, R55.2, R56.2, R57.2, R58.2, R59.2, R6.2, R60.2, R61.2, R62.2, R63.2, R64.2, R65.2, R66.2, R67.2, R68.2, R69.2, R7.2, R70.2, R71.2, R72.2, R73.2, R79.2, R8.2, R83.2, R87.2, R9.2, R91.2, R95.2, U2G$1.V+, VCC4.S, VCC5.S, VCC6.S
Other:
- note removed: "NMOS Logic Transistor Cell"
